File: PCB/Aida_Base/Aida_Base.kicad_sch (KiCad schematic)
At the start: 224 parts, among them J1 AudioJack4, J10 Conn_01x03_Pin, J11 Conn_01x04_Pin, J12 Conn_01x04_Pin, J13 Conn_01x04_Pin, J14 Conn_01x04_Pin, J15 Conn_01x04_Pin, J16 Conn_01x04_Pin, J17 Conn_02x02_Odd_Even, J18 Conn_02x02_Odd_Even, J2 AudioJack4, J3 USB_C_Receptacle_L, J4 USB_C_Receptacle_R, J5 Conn_01x02_Pin, J6 Conn_01x02_Pin, J7 Conn_01x05_Pin, J8 Conn_01x05_Pin, J9 Conn_01x03_Pin, Q1 BSS138, Q2 BSS138, SW1 BOOT, SW2 BOOT, SW3 RESET, SW4 RESET, U3 RP2040_L, U4 RP2040_R, U5 W25Q128JVS, U6 W25Q128JVS, U7 AP2112K-3.3, U8 AP2112K-3.3, Y1 12MHz, Y2 12MHz

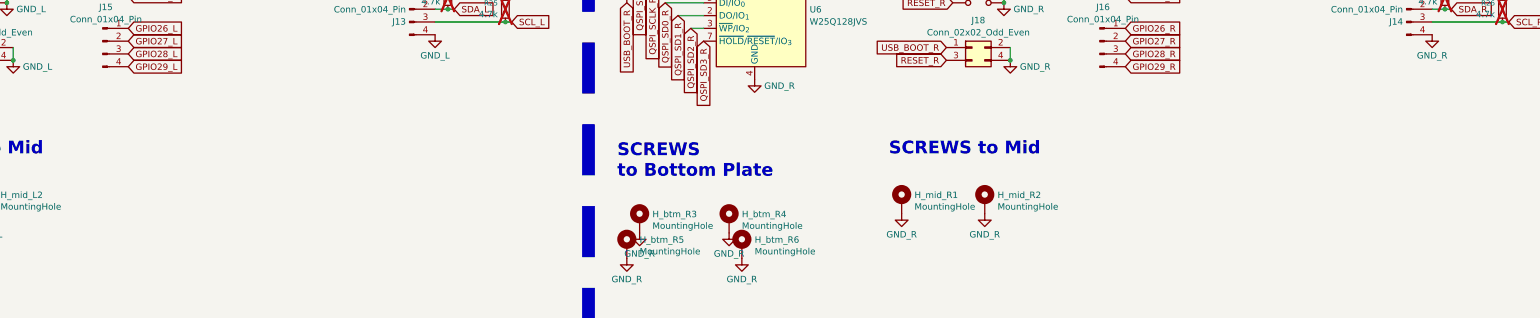
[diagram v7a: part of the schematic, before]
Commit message: マトリクス行列のテストポイント追加
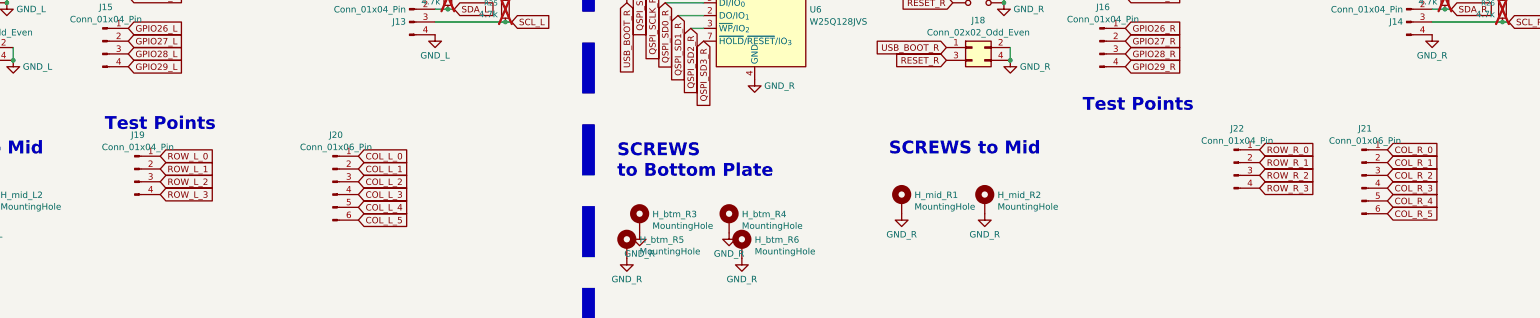
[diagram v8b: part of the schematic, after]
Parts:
- added J19, J22: Conn_01x04_Pin, Connector_PinHeader_2.00mm:PinHeader_1x04_P2.00mm_Vertical, symbol Connector:Conn_01x04_Pin
- added J20, J21: Conn_01x06_Pin, Connector_PinHeader_2.00mm:PinHeader_1x06_P2.00mm_Vertical, symbol Connector:Conn_01x06_Pin
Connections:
- net COL_L_0: now also J20.1 (Pin_1)
- net COL_L_1: now also J20.2 (Pin_2)
- net COL_L_2: now also J20.3 (Pin_3)
- net COL_L_3: now also J20.4 (Pin_4)
- net COL_L_4: now also J20.5 (Pin_5)
- net COL_L_5: now also J20.6 (Pin_6)
- net COL_R_0: now also J21.1 (Pin_1)
- net COL_R_1: now also J21.2 (Pin_2)
- net COL_R_2: now also J21.3 (Pin_3)
- net COL_R_3: now also J21.4 (Pin_4)
- net COL_R_4: now also J21.5 (Pin_5)
- net COL_R_5: now also J21.6 (Pin_6)
- net ROW_L_0: now also J19.1 (Pin_1)
- net ROW_L_1: now also J19.2 (Pin_2)
- net ROW_L_2: now also J19.3 (Pin_3)
- net ROW_L_3: now also J19.4 (Pin_4)
- net ROW_R_0: now also J22.1 (Pin_1)
- net ROW_R_1: now also J22.2 (Pin_2)
- net ROW_R_2: now also J22.3 (Pin_3)
- net ROW_R_3: now also J22.4 (Pin_4)
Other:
- note added: "Test Points"
